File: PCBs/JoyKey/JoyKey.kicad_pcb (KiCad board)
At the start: 2 copper layers, 90.2 x 55 mm, 55 parts, among them J1 OLED_DISPLAY, J2 Conn_01x03_Socket, J3 Testpad wire hole1, J4 JST PH, J5 Top Trigger 1, J6 Top Trigger 2, Q1 PMOS,Si7157DP, SW1 RotaryEncoder_Switch, SW2 SW_Push_45deg, SW3 SW_Push_45deg, SW4 SW_Push_45deg, SW5 SW_Push_45deg, SW6 SW_Push_45deg, SW7 SW_Push_45deg, U1 BQ25060, U3 XIAO-RP2040-DIP, U4 LP2981-3.3, U5 2_axis_analog_joystick_button

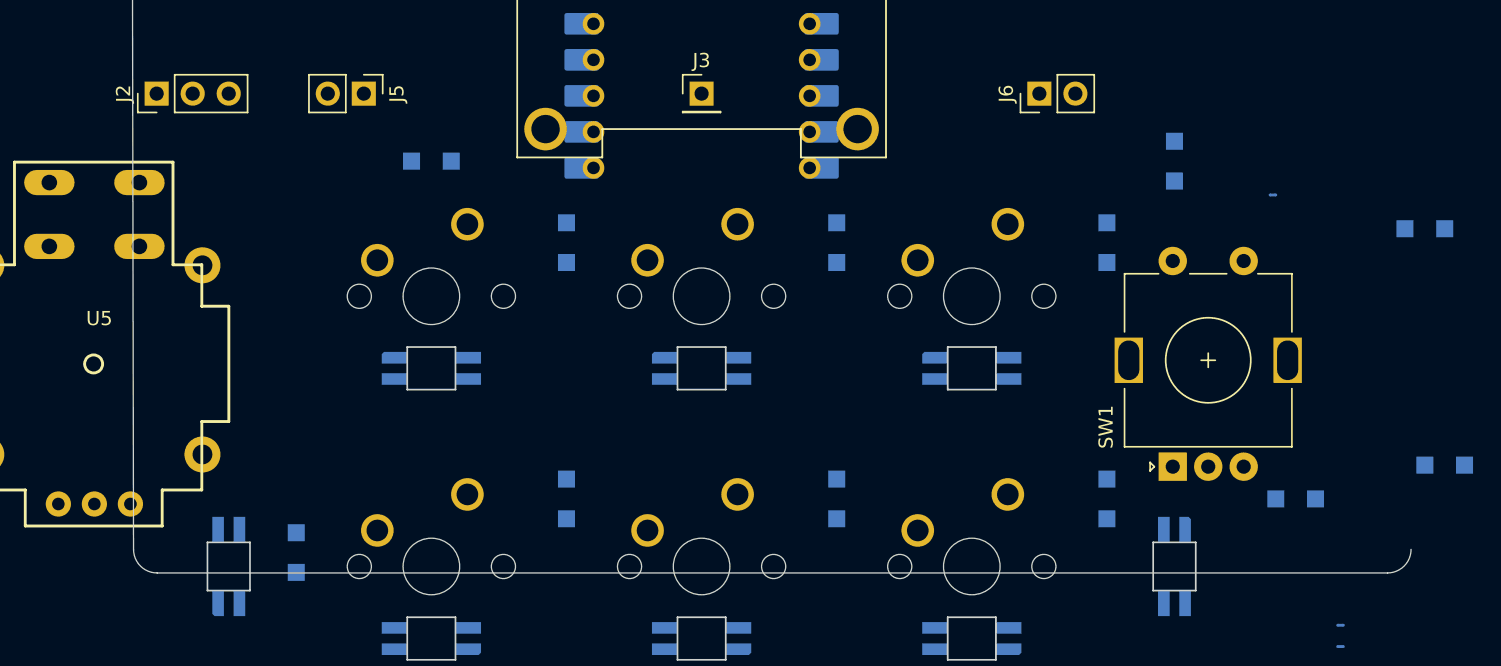
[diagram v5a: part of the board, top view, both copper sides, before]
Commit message: Re-arranged matrix to have L-shaped clusters
Based on my horizontal layout I really have a 6*2 matrix, however the most switches for the least pins is actually a 4*3. So, I have to great creative with my routing to make it fit.
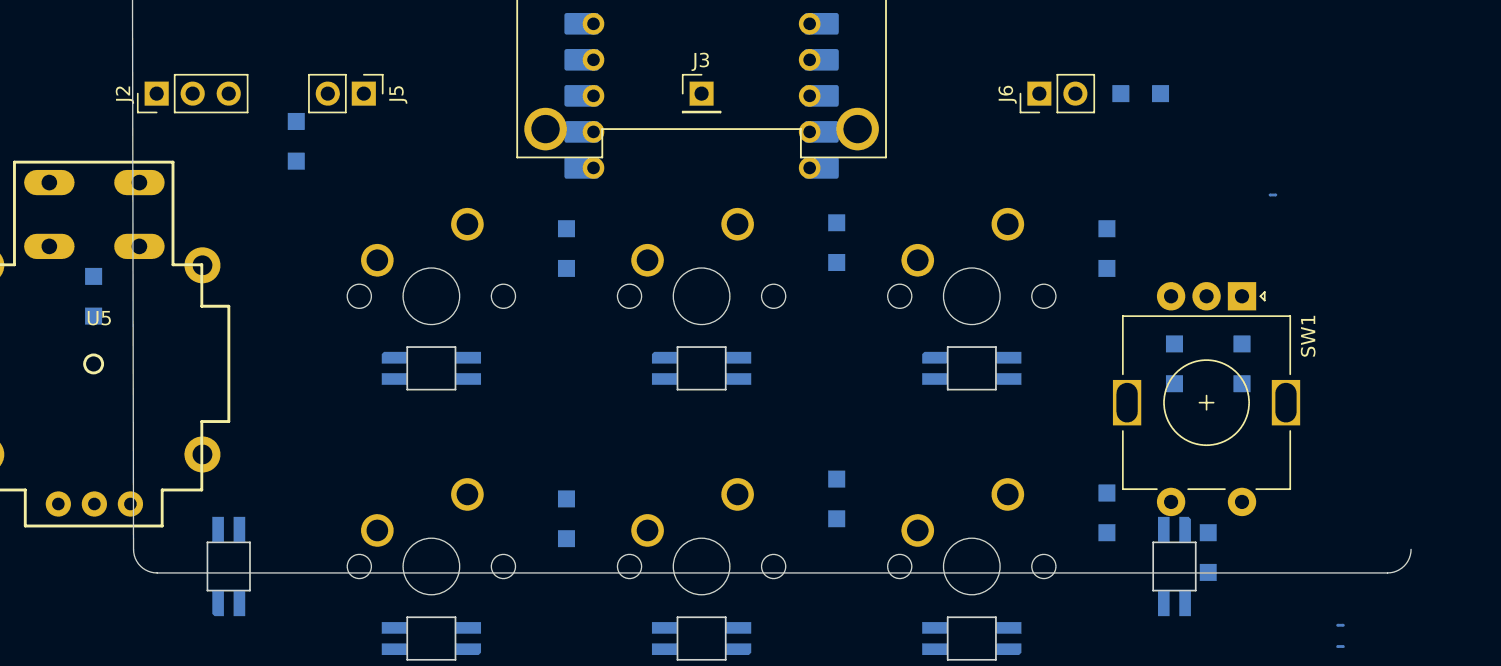
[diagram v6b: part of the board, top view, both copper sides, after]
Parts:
- removed the SW2 at (121.4, 109.5)
- added SW3: SW_Push_45deg, MX_Solderable:MX-Solderable-1U, F.Cu at (159.5, 109.5)
- moved D14 96.0 mm to (97.6, 109.5), turned to 90 degrees
- moved D17 64.3 mm to (176.2, 127.6)
- moved D15 51.4 mm to (131.0, 125.2), turned to 90 degrees
- moved D4 50.2 mm to (171.4, 95.2)
- moved SW6 38.1 mm to (121.4, 128.6)
- moved D16 30.1 mm to (169.1, 124.8), turned to 90 degrees
- moved D1 20.3 mm to (111.9, 98.6)
- moved SW4 19.1 mm to (121.4, 109.5)
- moved SW7 19.1 mm to (159.5, 128.6)
- moved D9 17.7 mm to (131.0, 106.2)
- moved D13 15.1 mm to (178.6, 114.3)
- moved SW1 13.0 mm to (178.6, 109.5), turned to -90 degrees
- moved D12 10.6 mm to (173.8, 114.3)
- moved D3 0.42 mm to (169.1, 106.2)
- renumbered SW3 to SW2
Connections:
- D12 pad 2: Net-(D12-A) -> /Analog Input/EC11B
- D13 pad 2: Net-(D13-A) -> /Analog Input/EC11A
- D14 pad 2: /Analog Input/EC11A -> /Analog Input/StickButtonB
- D15 pad 2: /Analog Input/EC11B -> Net-(D15-A)
- D16 pad 2: /Analog Input/EC11SWB -> Net-(D16-A)
- D17 pad 2: /Analog Input/StickButtonB -> /Analog Input/EC11SWB
- J5 pad 1: /COL3 -> /COL0
- J5 pad 2: Net-(D4-A) -> Net-(D1-A)
- J6 pad 2: Net-(D13-A) -> Net-(D4-A)
- NT1 pad 1: /Analog Input/EC11Common -> /Analog Input/StickButtonA
- NT2 pad 2: /COL1 -> /COL3
- NT3 pad 1: /Analog Input/EC11SWA -> /Analog Input/EC11Common
- NT4 pad 1: /Analog Input/StickButtonA -> /Analog Input/EC11SWA
- SW6 pad 1: /COL2 -> /COL1
- SW6 pad 2: Net-(D12-A) -> Net-(D15-A)
- SW7 pad 2: Net-(D3-A) -> Net-(D16-A)
- U3 pad 10: /COL2 -> /COL0
- U3 pad 4: /ROW0 -> /ROW2
- U3 pad 7: /ROW2 -> /ROW0
- U3 pad 8: /COL0 -> /COL2

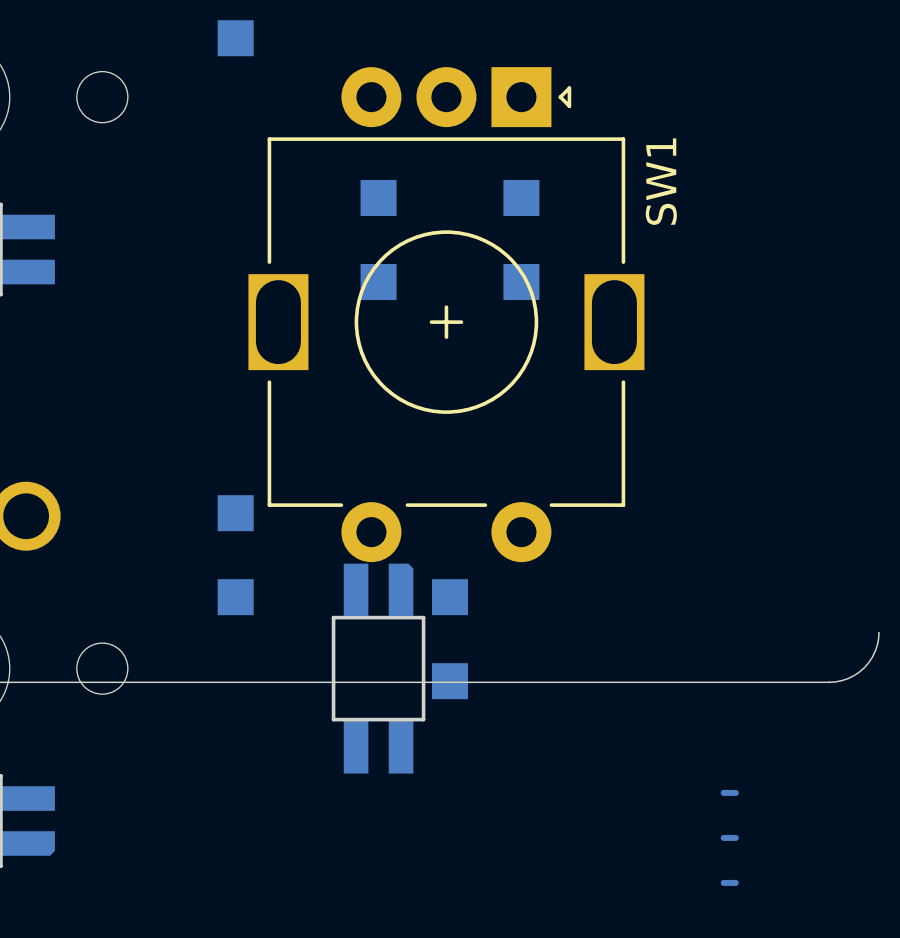
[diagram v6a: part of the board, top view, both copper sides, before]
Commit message: Fixed Encoder on Matrix (again)
I got it messed up, A and B should have separate power sources (columns) and common should go to the row. If I had vertical orientation I would have common be on the column and A and B on separate rows. Previous caused a short between columns that could cause ghosting.
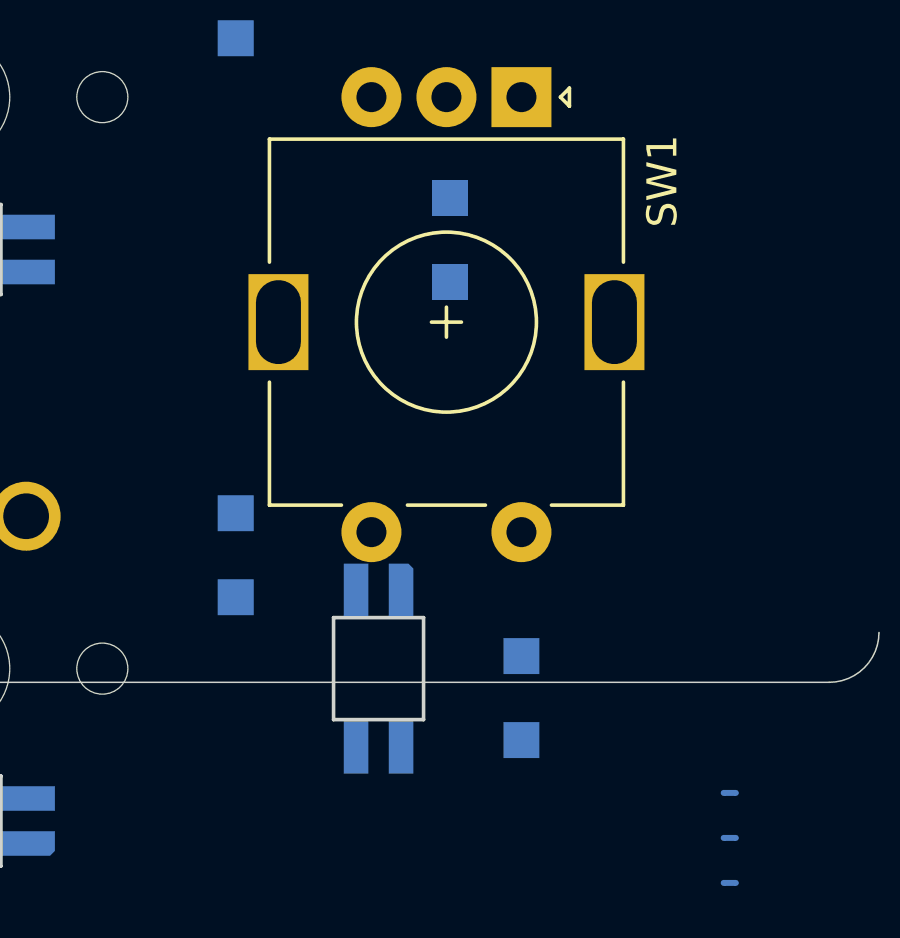
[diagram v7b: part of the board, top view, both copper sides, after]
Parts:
- removed D13: 1N4148W, Diode_SMD:Nexperia_CFP3_SOD-123W
- moved D17 3.09 mm to (178.6, 129.6)
- moved D12 2.38 mm to (176.2, 114.3)
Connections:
- D12 pad 2: /Analog Input/EC11B -> /Analog Input/EC11Common
- NT2 pad 1: /Analog Input/EC11Common -> /Analog Input/EC11A
- NT3 pad 1: /Analog Input/EC11Common -> /Analog Input/EC11B

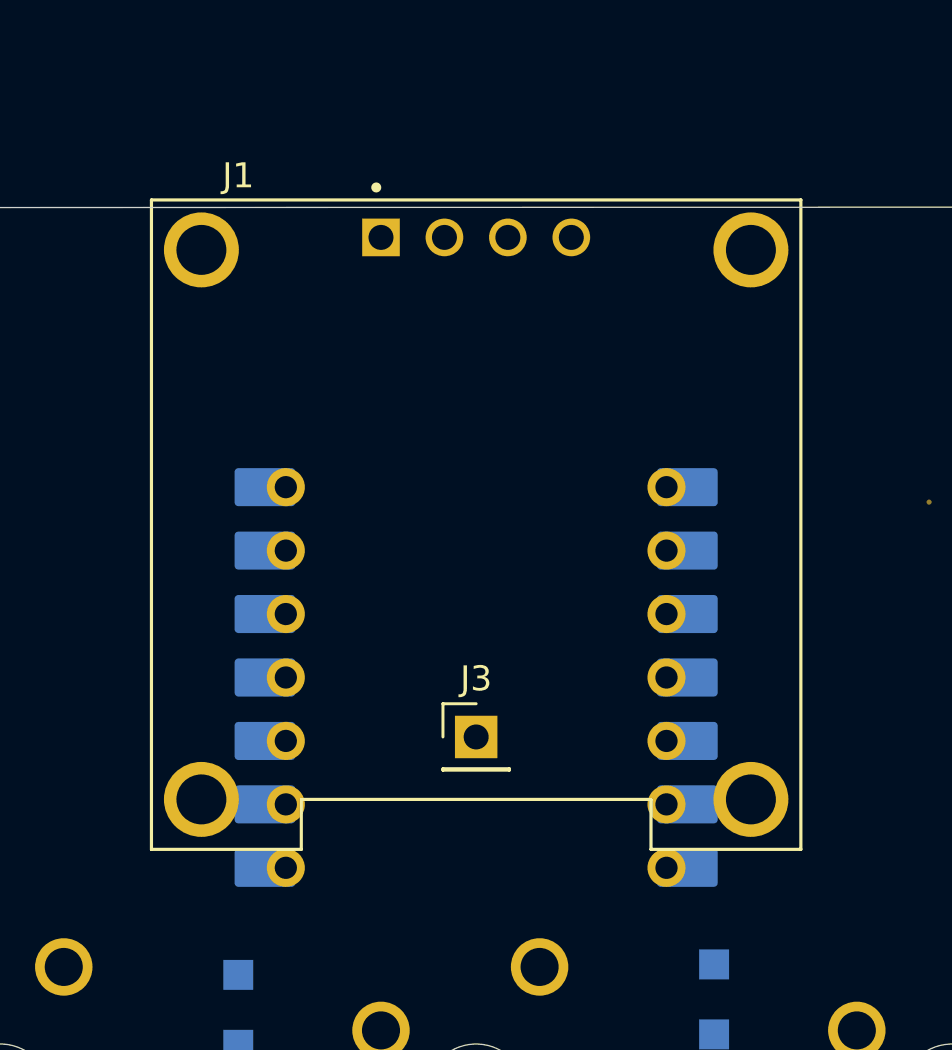
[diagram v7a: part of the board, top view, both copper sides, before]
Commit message: Removed Display Mounting holes
Annoying, and unneeded
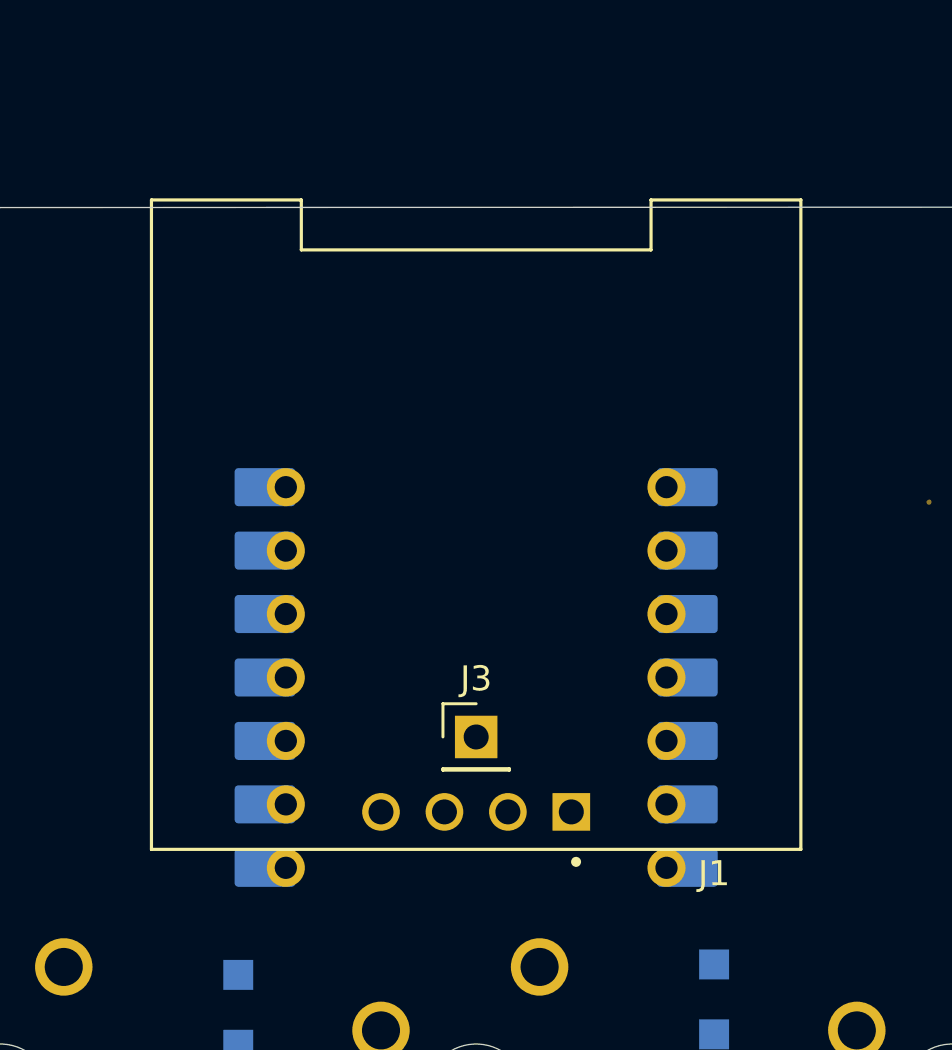
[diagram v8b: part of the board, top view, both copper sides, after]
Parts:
- turned J1 to 180 degrees
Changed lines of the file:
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@@
 	(footprint "SSD1306:SSD1306-OLED096-128x64"
 		(layer "F.Cu")
-		(at 140.49375 86.75)
+		(at 140.49375 86.75 180)
 		(property "Reference" "J1"
 			(at -9.525 -13.97 0)
@@
 		(attr through_hole)
 		(fp_line
+			(start 13 13)
+			(end 7 13)
+			(stroke
+				(width 0.127)
+				(type solid)
+			)
+			(layer "F.SilkS")
+		)
+		(fp_line
+			(start 13 -13)
+			(end 13 13)
+			(stroke
+				(width 0.127)
+				(type solid)
+			)
+			(layer "F.SilkS")
+		)
+		(fp_line
+			(start 7 13)
+			(end 7 11)
+			(stroke
+				(width 0.127)
+				(type solid)
+			)
+			(layer "F.SilkS")
+		)
+		(fp_line
+			(start 7 11)
+			(end -7 11)
+			(stroke
+				(width 0.127)
+				(type solid)
+			)
+			(layer "F.SilkS")
+		)
+		(fp_line
+			(start -7 13)
+			(end -13 13)
+			(stroke
+				(width 0.127)
+				(type solid)
+			)
+			(layer "F.SilkS")
+		)
+		(fp_line
+			(start -7 11)
+			(end -7 13)
+			(stroke
+				(width 0.127)
+				(type solid)
+			)
+			(layer "F.SilkS")
+		)
+		(fp_line
+			(start -13 13)
+			(end -13 -13)
+			(stroke
+				(width 0.127)
+				(type solid)
+			)
+			(layer "F.SilkS")
+		)
+		(fp_line
 			(start -13 -13)
 			(end 13 -13)
-			(stroke
-				(width 0.127)
-				(type solid)
-			)
-			(layer "F.SilkS")
-		)
-		(fp_line
-			(start -13 13)
-			(end -13 -13)
-			(stroke
-				(width 0.127)
-				(type solid)
-			)
-			(layer "F.SilkS")
-		)
-		(fp_line
-			(start -7 11)
-			(end -7 13)
-			(stroke
-				(width 0.127)
-				(type solid)
-			)
-			(layer "F.SilkS")
-		)
-		(fp_line
-			(start -7 13)
-			(end -13 13)
-			(stroke
-				(width 0.127)
-				(type solid)
-			)
-			(layer "F.SilkS")
-		)
-		(fp_line
-			(start 7 11)
-			(end -7 11)
-			(stroke
-				(width 0.127)
-				(type solid)
-			)
-			(layer "F.SilkS")
-		)
-		(fp_line
-			(start 7 13)
-			(end 7 11)
-			(stroke
-				(width 0.127)
-				(type solid)
-			)
-			(layer "F.SilkS")
-		)
-		(fp_line
-			(start 13 -13)
-			(end 13 13)
-			(stroke
-				(width 0.127)
-				(type solid)
-			)
-			(layer "F.SilkS")
-		)
-		(fp_line
-			(start 13 13)
-			(end 7 13)
 			(stroke
 				(width 0.127)
@@
 		)
 		(fp_line
+			(start 13.25 13.25)
+			(end -13.25 13.25)
+			(stroke
+				(width 0.05)
+				(type solid)
+			)
+			(layer "F.CrtYd")
+		)
+		(fp_line
+			(start 13.25 -13.25)
+			(end 13.25 13.25)
+			(stroke
+				(width 0.05)
+				(type solid)
+			)
+			(layer "F.CrtYd")
+		)
+		(fp_line
+			(start -13.25 13.25)
+			(end -13.25 -13.25)
+			(stroke
+				(width 0.05)
+				(type solid)
+			)
+			(layer "F.CrtYd")
+		)
+		(fp_line
 			(start -13.25 -13.25)
 			(end 13.25 -13.25)
@@
 		)
 		(fp_line
-			(start -13.25 13.25)
-			(end -13.25 -13.25)
-			(stroke
-				(width 0.05)
-				(type solid)
-			)
-			(layer "F.CrtYd")
-		)
-		(fp_line
-			(start 13.25 -13.25)
-			(end 13.25 13.25)
-			(stroke
-				(width 0.05)
-				(type solid)
-			)
-			(layer "F.CrtYd")
-		)
-		(fp_line
-			(start 13.25 13.25)
-			(end -13.25 13.25)
-			(stroke
-				(width 0.05)
-				(type solid)
-			)
-			(layer "F.CrtYd")
+			(start 13 13)
+			(end 7 13)
+			(stroke
+				(width 0.127)
+				(type solid)
+			)
+			(layer "F.Fab")
+		)
+		(fp_line
+			(start 13 -13)
+			(end 13 13)
+			(stroke
+				(width 0.127)
+				(type solid)
+			)
+			(layer "F.Fab")
+		)
+		(fp_line
+			(start 7 11)
+			(end 7 13)
+			(stroke
+				(width 0.127)
+				(type solid)
+			)
+			(layer "F.Fab")
+		)
+		(fp_line
+			(start -7 13)
+			(end -7 11)
+			(stroke
+				(width 0.127)
+				(type solid)
+			)
+			(layer "F.Fab")
+		)
+		(fp_line
+			(start -7 13)
+			(end -13 13)
+			(stroke
+				(width 0.127)
+				(type solid)
+			)
+			(layer "F.Fab")
+		)
+		(fp_line
+			(start -7 11)
+			(end 7 11)
+			(stroke
+				(width 0.127)
+				(type solid)
+			)
+			(layer "F.Fab")
+		)
+		(fp_line
+			(start -13 13)
+			(end -13 -13)
+			(stroke
+				(width 0.127)
+				(type solid)
+			)
+			(layer "F.Fab")
 		)
 		(fp_line
 			(start -13 -13)
 			(end 13 -13)
-			(stroke
-				(width 0.127)
-				(type solid)
-			)
-			(layer "F.Fab")
-		)
-		(fp_line
-			(start -13 13)
-			(end -13 -13)
-			(stroke
-				(width 0.127)
-				(type solid)
-			)
-			(layer "F.Fab")
-		)
-		(fp_line
-			(start -7 11)
-			(end 7 11)
-			(stroke
-				(width 0.127)
-				(type solid)
-			)
-			(layer "F.Fab")
-		)
-		(fp_line
-			(start -7 13)
-			(end -13 13)
-			(stroke
-				(width 0.127)
-				(type solid)
-			)
-			(layer "F.Fab")
-		)
-		(fp_line
-			(start -7 13)
-			(end -7 11)
-			(stroke
-				(width 0.127)
-				(type solid)
-			)
-			(layer "F.Fab")
-		)
-		(fp_line
-			(start 7 11)
-			(end 7 13)
-			(stroke
-				(width 0.127)
-				(type solid)
-			)
-			(layer "F.Fab")
-		)
-		(fp_line
-			(start 13 -13)
-			(end 13 13)
-			(stroke
-				(width 0.127)
-				(type solid)
-			)
-			(layer "F.Fab")
-		)
-		(fp_line
-			(start 13 13)
-			(end 7 13)
 			(stroke
 				(width 0.127)
@@
 		)
 		(pad "1" thru_hole rect
-			(at -3.81 -11.5)
+			(at -3.81 -11.5 180)
 			(size 1.508 1.508)
 			(drill 1)
@@
 		)
 		(pad "2" thru_hole circle
-			(at -1.27 -11.5)
+			(at -1.27 -11.5 180)
 			(size 1.508 1.508)
 			(drill 1)
@@
 		)
 		(pad "3" thru_hole circle
-			(at 1.27 -11.5)
+			(at 1.27 -11.5 180)
 			(size 1.508 1.508)
 			(drill 1)
@@
 		)
 		(pad "4" thru_hole circle
-			(at 3.81 -11.5)
+			(at 3.81 -11.5 180)
 			(size 1.508 1.508)
 			(drill 1)
@@
 			(solder_mask_margin 0.102)
 		)
-		(pad "S1" thru_hole circle
-			(at -11 -11)
-			(size 3 3)
-			(drill 2)
-			(layers "*.Cu" "*.Mask")
-			(remove_unused_layers no)
-			(solder_mask_margin 0.102)
-		)
-		(pad "S2" thru_hole circle
-			(at 11 -11)
-			(size 3 3)
-			(drill 2)
-			(layers "*.Cu" "*.Mask")
-			(remove_unused_layers no)
-			(solder_mask_margin 0.102)
-		)
-		(pad "S3" thru_hole circle
-			(at 11 11)
-			(size 3 3)
-			(drill 2)
-			(layers "*.Cu" "*.Mask")
-			(remove_unused_layers no)
-			(solder_mask_margin 0.102)
-		)
-		(pad "S4" thru_hole circle
-			(at -11 11)
-			(size 3 3)
-			(drill 2)
-			(layers "*.Cu" "*.Mask")
-			(remove_unused_layers no)
-			(solder_mask_margin 0.102)
-		)
